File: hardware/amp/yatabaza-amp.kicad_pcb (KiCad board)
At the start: 2 copper layers, 46.4 x 60.3 mm, 10 parts, among them P1 POWER, P10 L, P11 R, P2 HV, P3 R, P4 SUPPORT, P5 MONO, P7 POWER, P8 AUDIO, P9 L

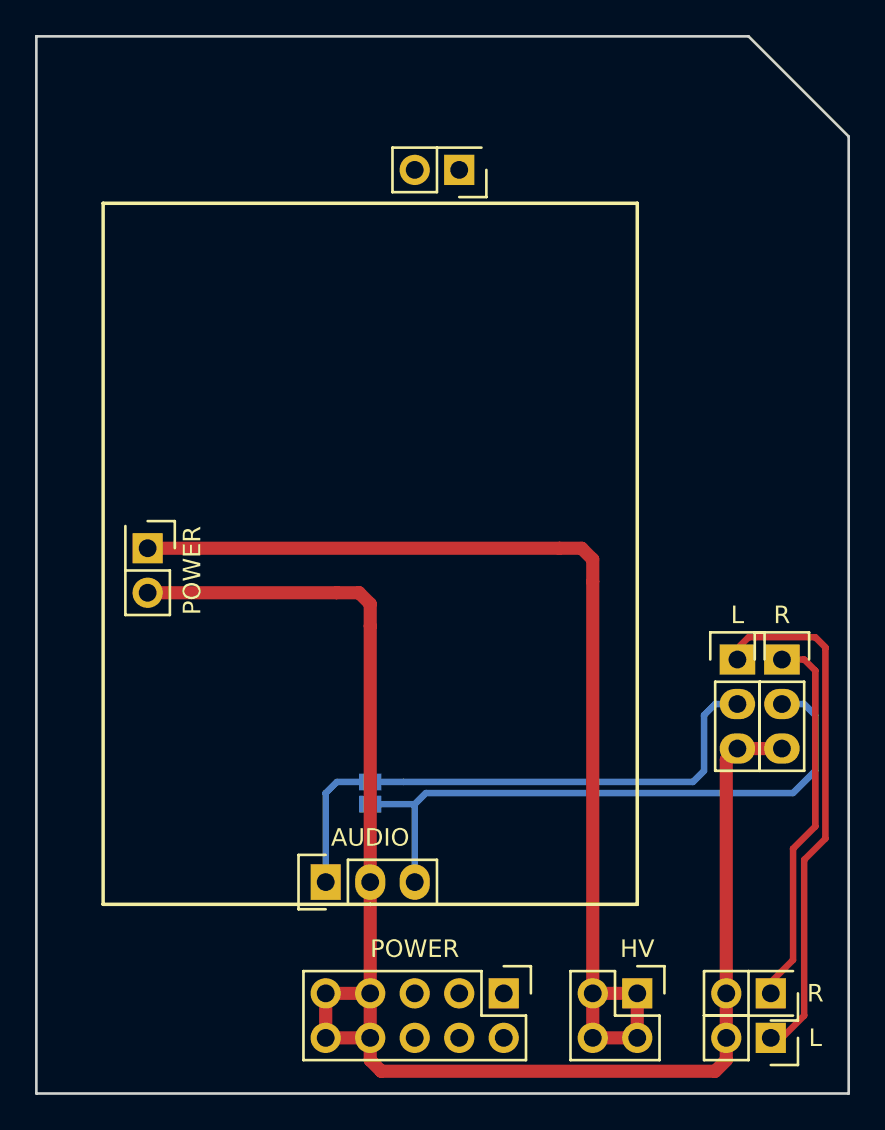
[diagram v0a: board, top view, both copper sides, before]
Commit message: ~ Ported hardware to Kicad6
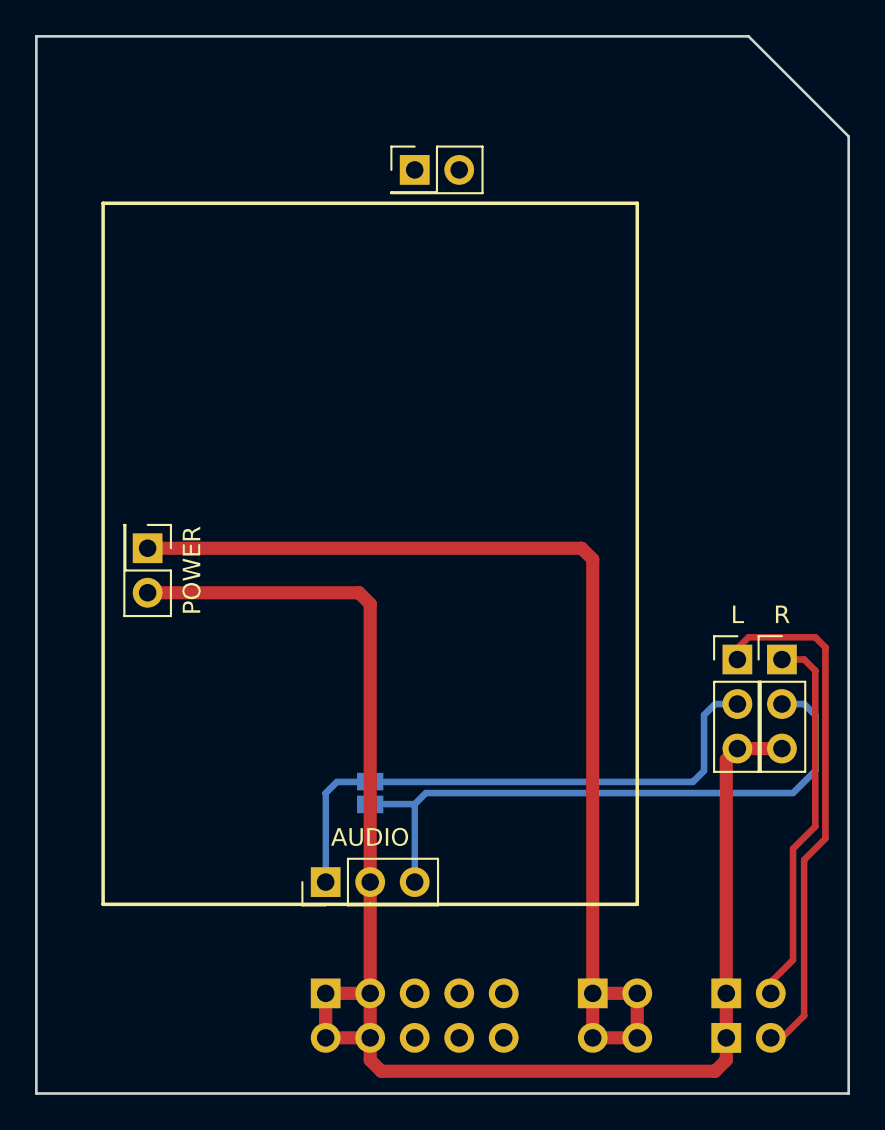
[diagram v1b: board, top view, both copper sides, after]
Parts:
- P1: footprint Pin_Headers:Pin_Header_Straight_2x05 -> Connector_PinHeader_2.54mm:PinHeader_2x05_P2.54mm_Vertical; moved to B.Cu
- P10, P11: footprint Pin_Headers:Pin_Header_Straight_2x01 -> Connector_PinHeader_2.54mm:PinHeader_1x02_P2.54mm_Vertical; moved to B.Cu
- P2: footprint Pin_Headers:Pin_Header_Straight_2x02 -> Connector_PinHeader_2.54mm:PinHeader_2x02_P2.54mm_Vertical; moved to B.Cu
- P3, P8, P9: footprint Pin_Headers:Pin_Header_Straight_1x03 -> Connector_PinHeader_2.54mm:PinHeader_1x03_P2.54mm_Vertical
- P4, P7: footprint Pin_Headers:Pin_Header_Straight_2x01 -> Connector_PinHeader_2.54mm:PinHeader_2x01_P2.54mm_Vertical
- P5: footprint Connect:GS2 -> Jumper:SolderJumper-2_P1.3mm_Open_Pad1.0x1.5mm
- moved P1 10.2 mm to (31.1, 66.7)
- moved P2 2.54 mm to (46.4, 66.7)
- moved P10 2.54 mm to (54.0, 69.2), turned to -90 degrees
- moved P11 2.54 mm to (54.0, 66.7), turned to -90 degrees
- moved P4 2.54 mm to (36.2, 19.7), turned to 0 degrees
- turned P5 to 90 degrees
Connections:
- P1 pad 1: Net-(P1-Pad1) -> GND
- P1 pad 10: GND -> unconnected-(P1-Pad10)
- P1 pad 2: Net-(P1-Pad2) -> GND
- P1 pad 3: Net-(P1-Pad3) -> GND
- P1 pad 4: Net-(P1-Pad4) -> GND
- P1 pad 5: Net-(P1-Pad5) -> unconnected-(P1-Pad5)
- P1 pad 6: Net-(P1-Pad6) -> unconnected-(P1-Pad6)
- P1 pad 7: GND -> unconnected-(P1-Pad7)
- P1 pad 8: GND -> unconnected-(P1-Pad8)
- P1 pad 9: GND -> unconnected-(P1-Pad9)
- P10 pad 1: Net-(P10-Pad1) -> GND
- P10 pad 2: GND -> Net-(P9-Pad1)
- P11 pad 1: Net-(P11-Pad1) -> GND
- P11 pad 2: GND -> Net-(P3-Pad1)
- P3 pad 1: Net-(P11-Pad1) -> Net-(P3-Pad1)
- P4 pad 1: Net-(P4-Pad1) -> unconnected-(P4-Pad1)
- P4 pad 2: Net-(P4-Pad2) -> unconnected-(P4-Pad2)
- P9 pad 1: Net-(P10-Pad1) -> Net-(P9-Pad1)
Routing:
- net Net-(P9-Pad1): track 0.00 -> 30.1 mm
- net Net-(P10-Pad1): track 30.1 -> 0.00 mm
- net Net-(P3-Pad1): track 0.00 -> 21.6 mm
- net Net-(P11-Pad1): track 21.6 -> 0.00 mm
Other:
- net class Default removed
- rule pad_to_mask_clearance: 0.2 -> 0
